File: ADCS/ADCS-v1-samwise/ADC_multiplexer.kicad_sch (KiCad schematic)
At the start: 3 parts, among them U9 ADS7830

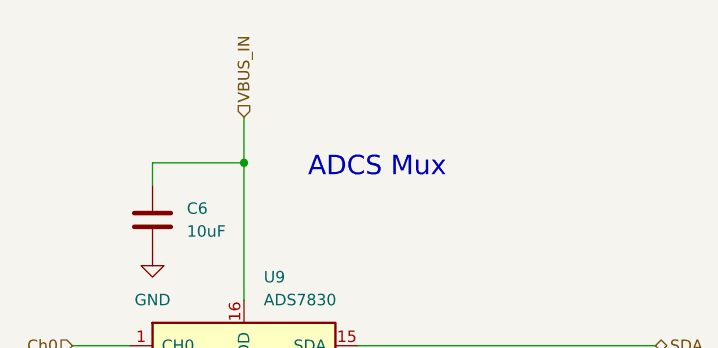
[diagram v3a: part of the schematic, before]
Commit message: Swap sun pyramid / photodiode yz inputs
Swap sun pyramid / photodiode yz inputs
 - Sun pyramids (8) -> RP3250B ADC pins
 - Photodiode yz (8) -> ADS7830 ADC
 - Logic behind this: RP2350B ADC has higher fidelity than ADS7830, and the yz photodiodes point in redundant directions so that's a waste.
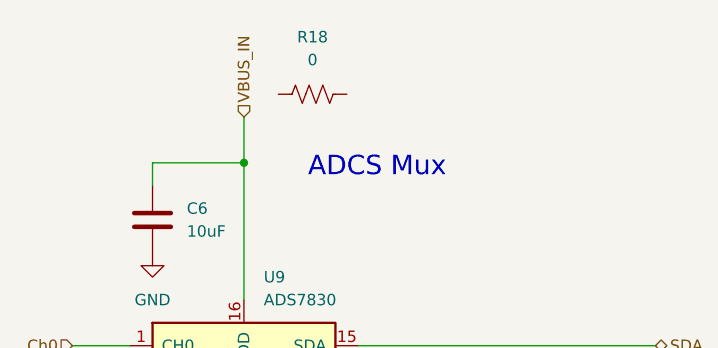
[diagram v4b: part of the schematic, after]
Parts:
- added R18: 0, Resistor_SMD:R_0603_1608Metric, symbol Device:R_US
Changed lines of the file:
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@@
+	)
+	(symbol
+		(lib_id "Device:R_US")
+		(at 166.37 82.55 90)
+		(unit 1)
+		(exclude_from_sim no)
+		(in_bom yes)
+		(on_board yes)
+		(dnp no)
+		(fields_autoplaced yes)
+		(property "Reference" "R18"
+			(at 166.37 76.2 90)
+			(effects
+				(font
+					(size 1.27 1.27)
+				)
+			)
+		)
+		(property "Value" "0"
+			(at 166.37 78.74 90)
+			(effects
+				(font
+					(size 1.27 1.27)
+				)
+			)
+		)
+		(property "Footprint" "Resistor_SMD:R_0603_1608Metric"
+			(at 166.624 81.534 90)
+			(effects
+				(font
+					(size 1.27 1.27)
+				)
+				(hide yes)
+			)
+		)
+		(property "Datasheet" "~"
+			(at 166.37 82.55 0)
+			(effects
+				(font
+					(size 1.27 1.27)
+				)
+				(hide yes)
+			)
+		)
+		(property "Description" "Resistor, US symbol"
+			(at 166.37 82.55 0)
+			(effects
+				(font
+					(size 1.27 1.27)
+				)
+				(hide yes)
+			)
+		)
+		(property "Height" ""
+			(at 166.37 82.55 0)
+			(effects
+				(font
+					(size 1.27 1.27)
+				)
+				(hide yes)
+			)
+		)
+		(pin "1"
+		)
+		(pin "2"
+		)
+		(instances
+			(project "ADCS_board"
+				(path "/db20b18b-d25a-428e-8229-70a189e1de75/00000000-0000-0000-0000-00005cec5a72/64c9d02f-f2a5-4afc-bcbd-2b44a6c6a2d8"
+					(reference "R18")
+					(unit 1)
+				)
+				(path "/db20b18b-d25a-428e-8229-70a189e1de75/00000000-0000-0000-0000-00005cec5a72/67beb92b-917b-42f4-9398-707556a28567"
+					(reference "R19")
+					(unit 1)
+				)
+			)
+		)
 	)
 	(symbol

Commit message: Revert "Swap sun pyramid / photodiode yz inputs"
This reverts commit 476f3e609712227db83ea3ec49a2480c44b72f0a.
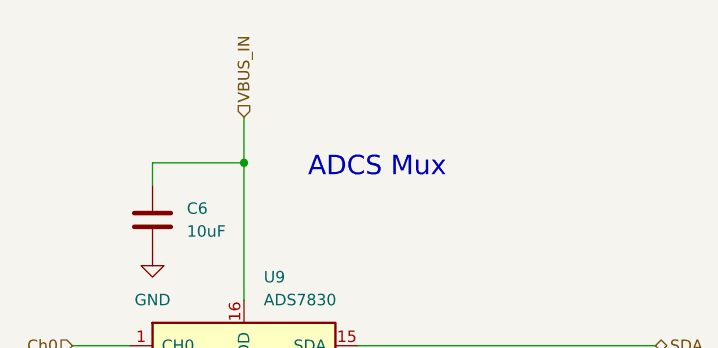
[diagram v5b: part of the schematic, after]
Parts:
- removed R18: 0, Resistor_SMD:R_0603_1608Metric, symbol Device:R_US
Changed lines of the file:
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@@
-	)
-	(symbol
-		(lib_id "Device:R_US")
-		(at 166.37 82.55 90)
-		(unit 1)
-		(exclude_from_sim no)
-		(in_bom yes)
-		(on_board yes)
-		(dnp no)
-		(fields_autoplaced yes)
-		(property "Reference" "R18"
-			(at 166.37 76.2 90)
-			(effects
-				(font
-					(size 1.27 1.27)
-				)
-			)
-		)
-		(property "Value" "0"
-			(at 166.37 78.74 90)
-			(effects
-				(font
-					(size 1.27 1.27)
-				)
-			)
-		)
-		(property "Footprint" "Resistor_SMD:R_0603_1608Metric"
-			(at 166.624 81.534 90)
-			(effects
-				(font
-					(size 1.27 1.27)
-				)
-				(hide yes)
-			)
-		)
-		(property "Datasheet" "~"
-			(at 166.37 82.55 0)
-			(effects
-				(font
-					(size 1.27 1.27)
-				)
-				(hide yes)
-			)
-		)
-		(property "Description" "Resistor, US symbol"
-			(at 166.37 82.55 0)
-			(effects
-				(font
-					(size 1.27 1.27)
-				)
-				(hide yes)
-			)
-		)
-		(property "Height" ""
-			(at 166.37 82.55 0)
-			(effects
-				(font
-					(size 1.27 1.27)
-				)
-				(hide yes)
-			)
-		)
-		(pin "1"
-		)
-		(pin "2"
-		)
-		(instances
-			(project "ADCS_board"
-				(path "/db20b18b-d25a-428e-8229-70a189e1de75/00000000-0000-0000-0000-00005cec5a72/64c9d02f-f2a5-4afc-bcbd-2b44a6c6a2d8"
-					(reference "R18")
-					(unit 1)
-				)
-				(path "/db20b18b-d25a-428e-8229-70a189e1de75/00000000-0000-0000-0000-00005cec5a72/67beb92b-917b-42f4-9398-707556a28567"
-					(reference "R19")
-					(unit 1)
-				)
-			)
-		)
 	)
 	(symbol

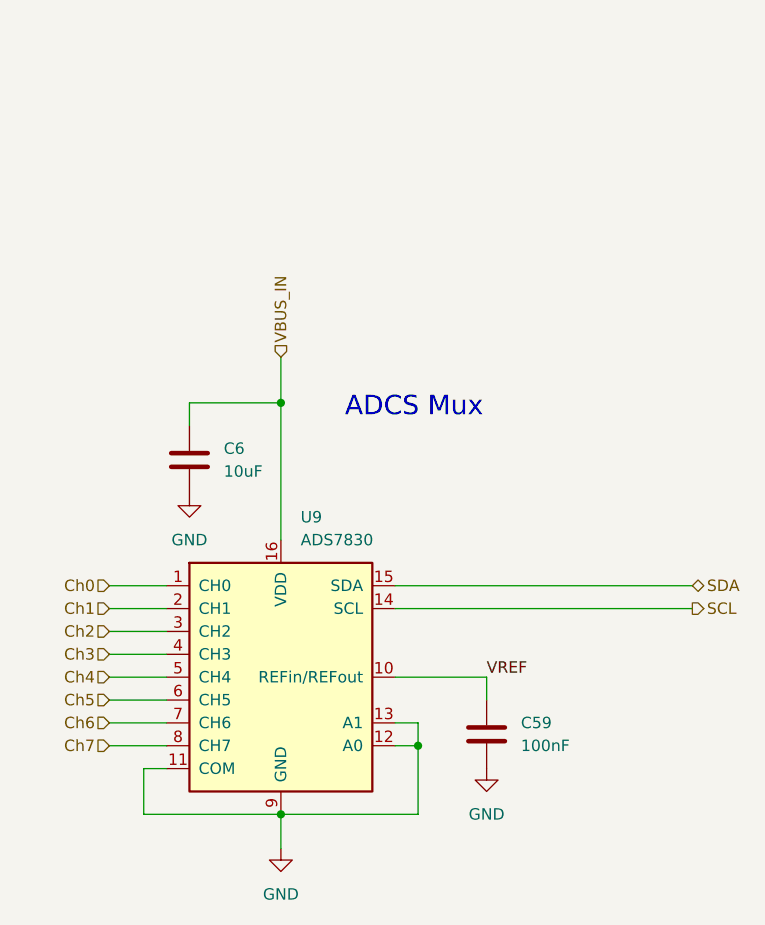
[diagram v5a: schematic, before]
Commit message: Sun sensor fixes (schematic)
1. Swap sun pyramid / photodiode yz inputs
 - Sun pyramids (8) -> RP3250B ADC pins
 - Photodiode yz (8) -> ADS7830 ADC
 - Logic behind this: RP2350B ADC has higher fidelity than ADS7830, and the yz photodiodes point in redundant directions so that's a waste.

2. Add 3.3v reference voltage to ADS7830
 - V_REF_RP2350B_ADC = 3.3v (can't change), V_REF_ADS7830 = 2.5v (internal)
 - This requires us to clip readings from the RP2350B ADC in the code
 - Since the ADS7830 can accept an external reference voltage, I've connected it up to the 3.3v bus to circumvent those reading issues :)

referenced adafruit ads7830 breakout board circuit for edits (link)[https://github.com/adafruit/Adafruit-ADS7830-PCB/tree/main]
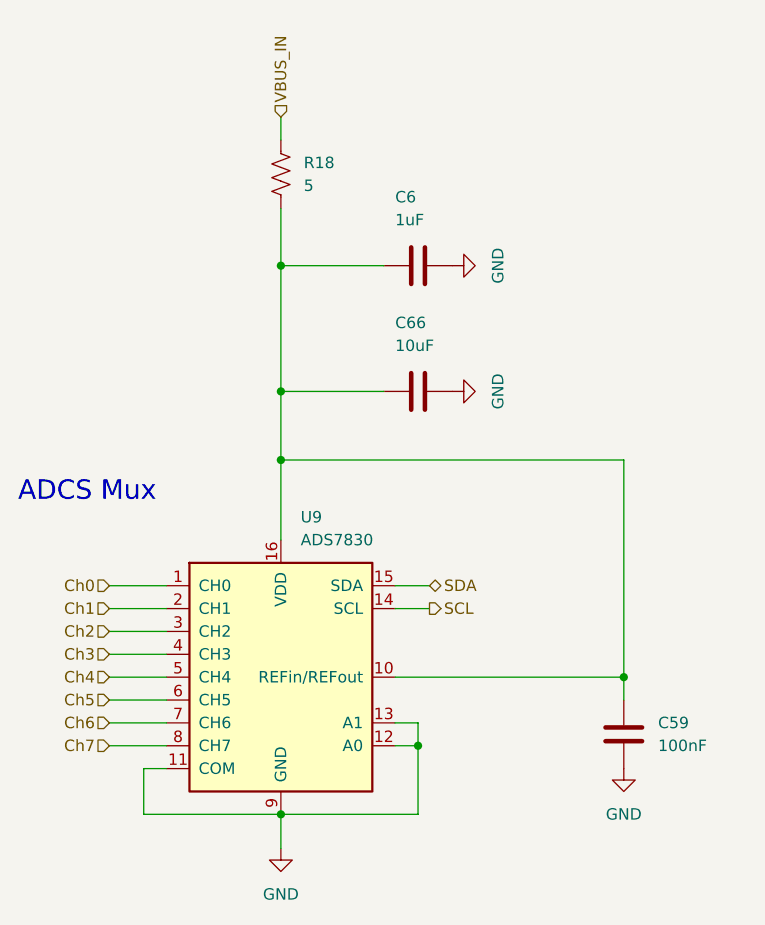
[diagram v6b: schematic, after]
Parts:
- added C66: 10uF, Capacitor_SMD:C_0603_1608Metric, symbol Device:C
- added R18: 5, Resistor_SMD:R_0603_1608Metric, symbol Device:R_US
- C6: value 10uF -> 1uF
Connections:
- net GND: now also C66.2
- net VBUS_IN: now also R18.1; no longer C6.1, U9.16 (VDD)
- net VREF: no longer names the net of C59.1, U9.10 (REFin/REFout)
- net VREF: now also C6.1, U9.16 (VDD), C66.1, R18.2
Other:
- moved on the sheet: C59, C6

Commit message: PD Rerouting + 3v3 external reference voltage
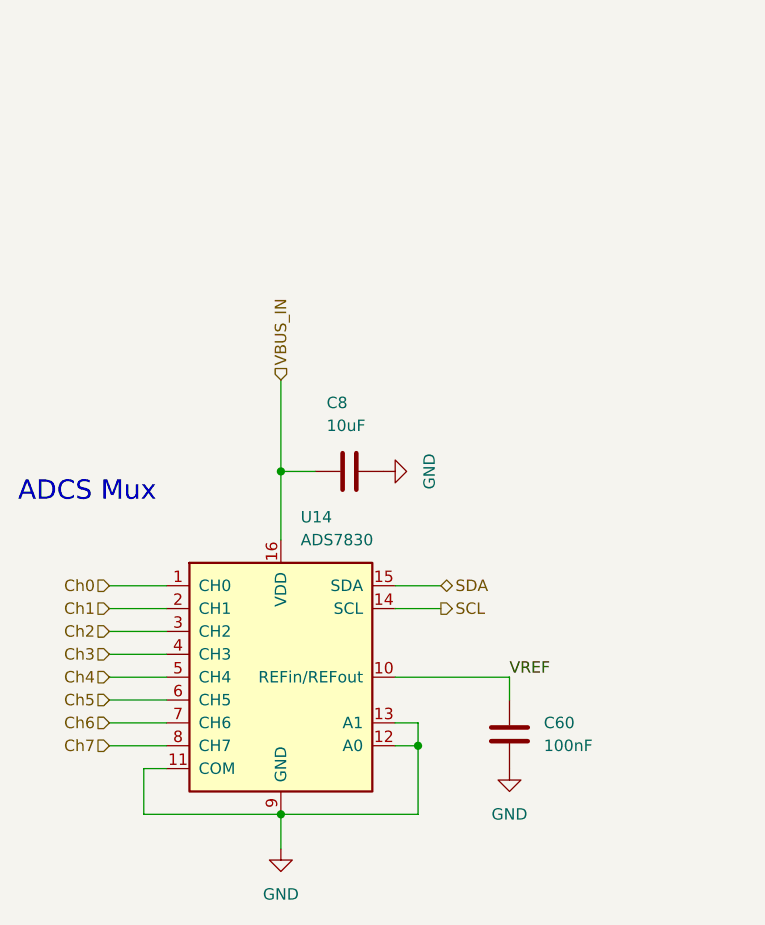
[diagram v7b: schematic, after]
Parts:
- removed C59: 100nF, Capacitor_SMD:C_0603_1608Metric, symbol Device:C
- removed C6: 1uF, Capacitor_SMD:C_0603_1608Metric, symbol Device:C
- removed C66: 10uF, Capacitor_SMD:C_0603_1608Metric, symbol Device:C
- removed R18: 5, Resistor_SMD:R_0603_1608Metric, symbol Device:R_US
- removed U9: ADS7830, Package_SO:TSSOP-16_4.4x5mm_P0.65mm, symbol Analog_DAC:ADS7830
- added C60: 100nF, Capacitor_SMD:C_0603_1608Metric, symbol Device:C
- added C8: 10uF, Capacitor_SMD:C_0603_1608Metric, symbol Device:C
- added U14: ADS7830, Package_SO:TSSOP-16_4.4x5mm_P0.65mm, symbol Analog_DAC:ADS7830
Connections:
- net Ch0: now also U14.1 (CH0)
- net Ch1: now also U14.2 (CH1)
- net Ch2: now also U14.3 (CH2)
- net Ch3: now also U14.4 (CH3)
- net Ch4: now also U14.5 (CH4)
- net Ch5: now also U14.6 (CH5)
- net Ch6: now also U14.7 (CH6)
- net Ch7: now also U14.8 (CH7)
- net GND: now also C60.2, C8.2, U14.11 (COM), U14.12 (A0), U14.13 (A1), U14.9 (GND)
- net SCL: now also U14.14 (SCL)
- net SDA: now also U14.15 (SDA)
- net VBUS_IN: now also C8.1, U14.16 (VDD)
- new net VREF: C60.1, U14.10 (REFin/REFout)
